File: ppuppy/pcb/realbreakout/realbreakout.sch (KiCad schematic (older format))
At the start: 18 parts, among them J1 Conn_01x36, J10 BCM11, J11 BCM13, J2 Conn_01x36, J3 Conn_01x36, J4 BCM25, J5 BCM24, J6 BCM27, J7 3V, J8 GND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

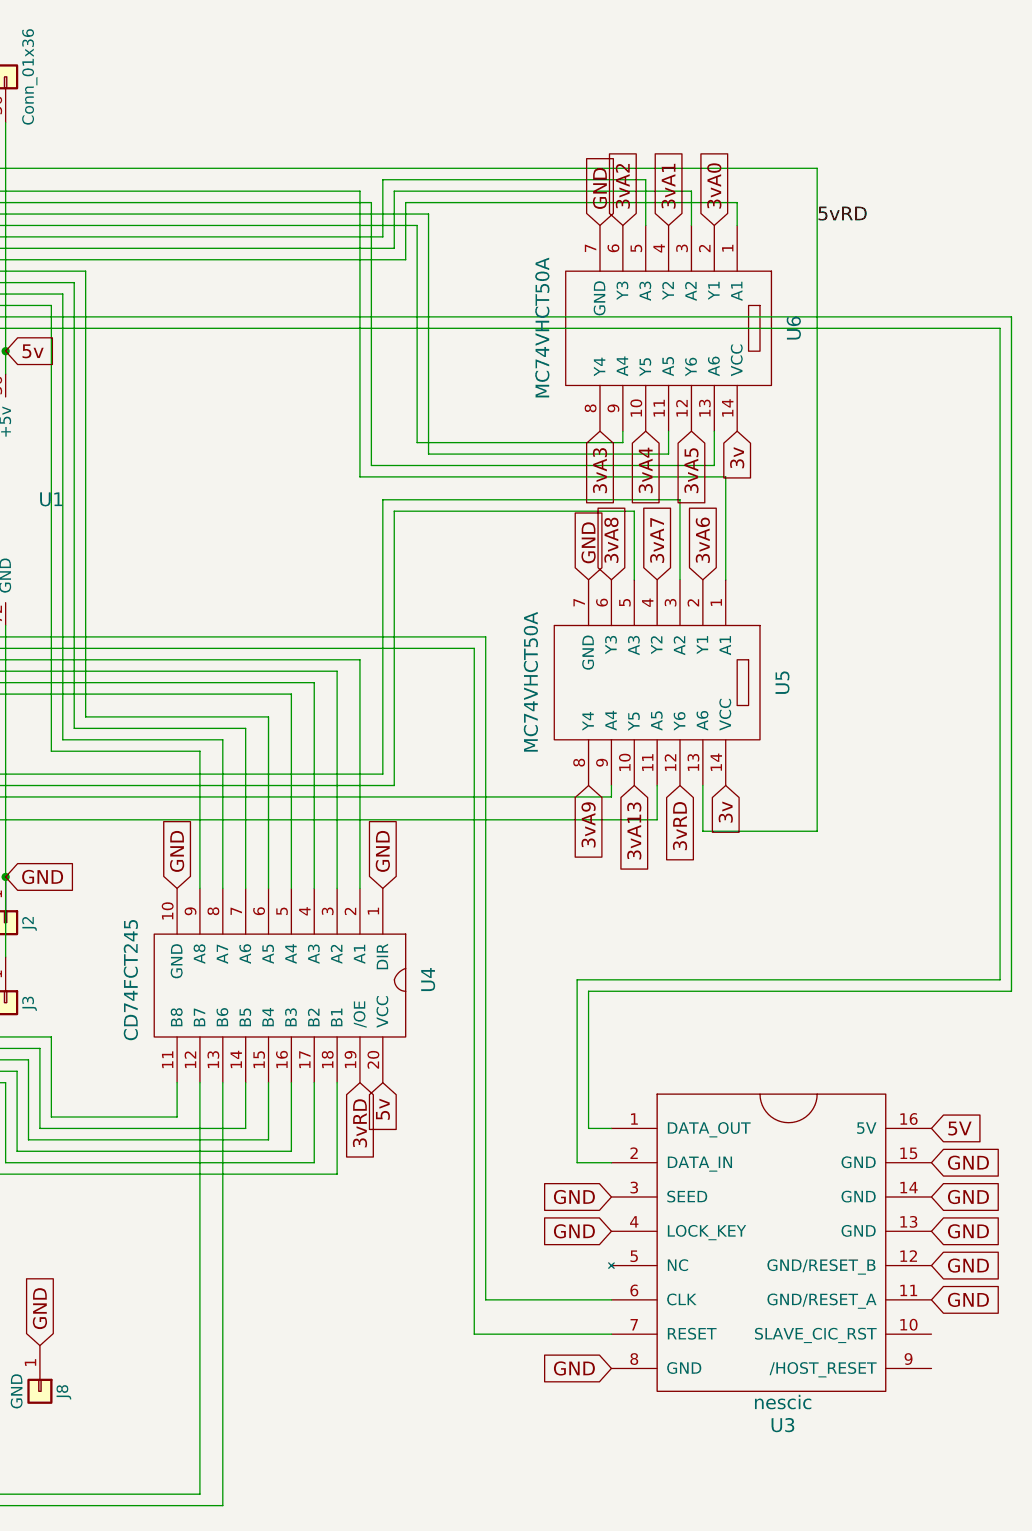
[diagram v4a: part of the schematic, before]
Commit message: Re-commit this stuff, which sourceforge lost (restoring a backup?\!?)
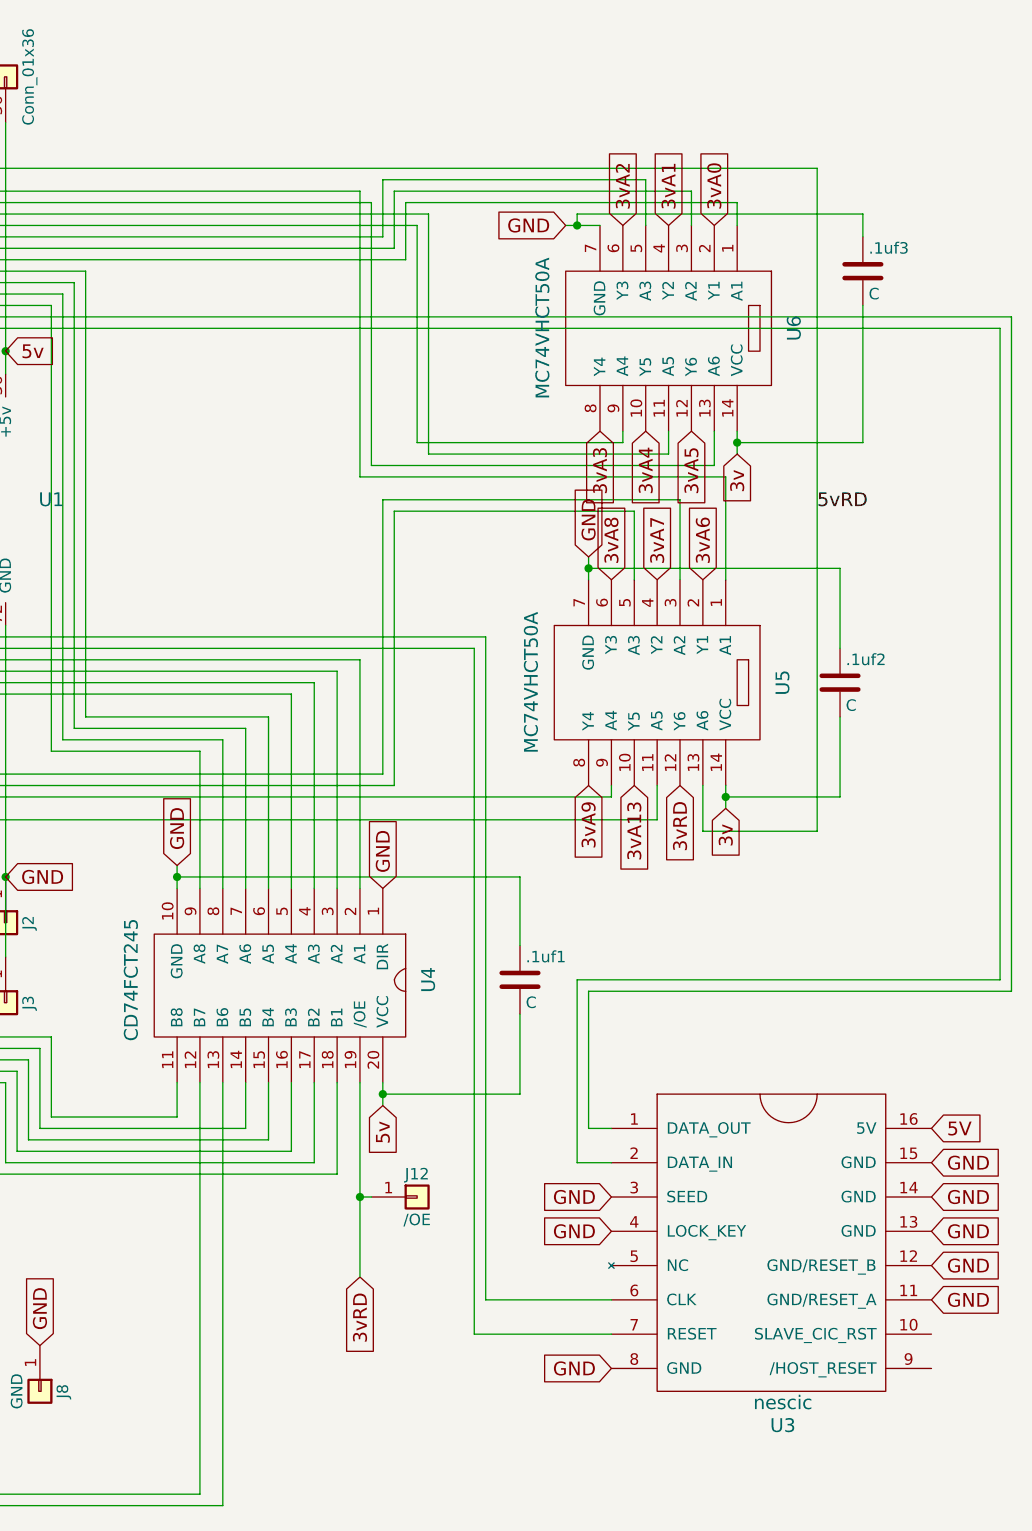
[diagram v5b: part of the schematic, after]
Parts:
- added .1uf1, .1uf2, .1uf3: C, Capacitors_THT:C_Disc_D5.0mm_W2.5mm_P5.00mm, symbol C
- added J12: /OE, Pin_Headers:Pin_Header_Straight_1x01_Pitch2.54mm, symbol Conn_01x01
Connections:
- net 3v: now also .1uf2.2, .1uf3.2
- net 3vRD: now also J12.1 (Pin_1)
- net 5v: now also .1uf1.2
- net GND: now also .1uf1.1, .1uf2.1, .1uf3.1
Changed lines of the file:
@@
 	0    1    1    0
 $EndComp
-Text GLabel 7450 3700 1    60   Input ~ 0
+Text GLabel 7450 3600 1    60   Input ~ 0
 GND
-Text GLabel 8350 4550 3    60   Input ~ 0
+Text GLabel 8350 4650 3    60   Input ~ 0
 5v
 Text GLabel 2150 1550 1    60   Input ~ 0
@@
 	0    1    1    0
 $EndComp
-Text GLabel 9900 1700 3    60   Input ~ 0
+Text GLabel 9900 1800 3    60   Input ~ 0
 3v
-Text GLabel 9850 3250 3    60   Input ~ 0
+Text GLabel 9850 3350 3    60   Input ~ 0
 3v
-Text GLabel 9250 2350 1    60   Input ~ 0
+Text GLabel 9250 2250 1    60   Input ~ 0
 GND
-Text GLabel 9300 800  1    60   Input ~ 0
+Text GLabel 9150 800  0    60   Input ~ 0
 GND
 Wire Wire Line
@@
 Text GLabel 5100 4700 1    60   Input ~ 0
 3v
-Text GLabel 8250 4550 3    60   Input ~ 0
+Text GLabel 8250 5400 3    60   Input ~ 0
 3vRD
 Wire Wire Line
@@
 Wire Wire Line
 	9750 3450 9750 3250
-Text Label 10250 800  0    60   ~ 0
+Text Label 10250 2050 0    60   ~ 0
 5vRD
 Text Label 1900 3300 0    60   ~ 0
@@
 Wire Wire Line
 	5000 4600 5000 4700
+$Comp
+L C .1uf2
+U 1 1 5AE8FA00
+P 10350 2800
+F 0 ".1uf2" H 10375 2900 50  0000 L CNN
+F 1 "C" H 10375 2700 50  0000 L CNN
+F 2 "Capacitors_THT:C_Disc_D5.0mm_W2.5mm_P5.00mm" H 10388 2650 50  0001 C CNN
+F 3 "" H 10350 2800 50  0001 C CNN
+	1    10350 2800
+	1    0    0    -1
+$EndComp
+Wire Wire Line
+	9850 3350 9850 3250
+Connection ~ 9850 3300
+Wire Wire Line
+	9850 3300 10350 3300
+Wire Wire Line
+	10350 3300 10350 2950
+Wire Wire Line
+	9250 2250 9250 2350
+Connection ~ 9250 2300
+Wire Wire Line
+	9250 2300 10350 2300
+Wire Wire Line
+	10350 2300 10350 2650
+Wire Wire Line
+	9150 800  9300 800
+Connection ~ 9200 800
+$Comp
+L C .1uf3
+U 1 1 5AE9096D
+P 10450 1000
+F 0 ".1uf3" H 10475 1100 50  0000 L CNN
+F 1 "C" H 10475 900 50  0000 L CNN
+F 2 "Capacitors_THT:C_Disc_D5.0mm_W2.5mm_P5.00mm" H 10488 850 50  0001 C CNN
+F 3 "" H 10450 1000 50  0001 C CNN
+	1    10450 1000
+	1    0    0    -1
+$EndComp
+Wire Wire Line
+	9900 1800 9900 1700
+Connection ~ 9900 1750
+Wire Wire Line
+	9900 1750 10450 1750
+Wire Wire Line
+	10450 1750 10450 1150
+Wire Wire Line
+	10450 850  10450 750
+Wire Wire Line
+	10450 750  9200 750
+Wire Wire Line
+	9200 750  9200 800
+Wire Wire Line
+	8350 4650 8350 4550
+Wire Wire Line
+	7450 3700 7450 3600
+Connection ~ 7450 3650
+Connection ~ 8350 4600
+$Comp
+L C .1uf1
+U 1 1 5AE9161B
+P 8950 4100
+F 0 ".1uf1" H 8975 4200 50  0000 L CNN
+F 1 "C" H 8975 4000 50  0000 L CNN
+F 2 "Capacitors_THT:C_Disc_D5.0mm_W2.5mm_P5.00mm" H 8988 3950 50  0001 C CNN
+F 3 "" H 8950 4100 50  0001 C CNN
+	1    8950 4100
+	1    0    0    -1
+$EndComp
+Wire Wire Line
+	7450 3650 8950 3650
+Wire Wire Line
+	8950 3650 8950 3950
+Wire Wire Line
+	8350 4600 8950 4600
+Wire Wire Line
+	8950 4600 8950 4250
+$Comp
+L Conn_01x01 J12
+U 1 1 5AE92E68
+P 8500 5050
+F 0 "J12" H 8500 5150 50  0000 C CNN
+F 1 "/OE" H 8500 4950 50  0000 C CNN
+F 2 "Pin_Headers:Pin_Header_Straight_1x01_Pitch2.54mm" H 8500 5050 50  0001 C CNN
+F 3 "" H 8500 5050 50  0001 C CNN
+	1    8500 5050
+	1    0    0    -1
+$EndComp
+Wire Wire Line
+	8250 4550 8250 5400
+Wire Wire Line
+	8300 5050 8250 5050
+Connection ~ 8250 5050
 $EndSCHEMATC

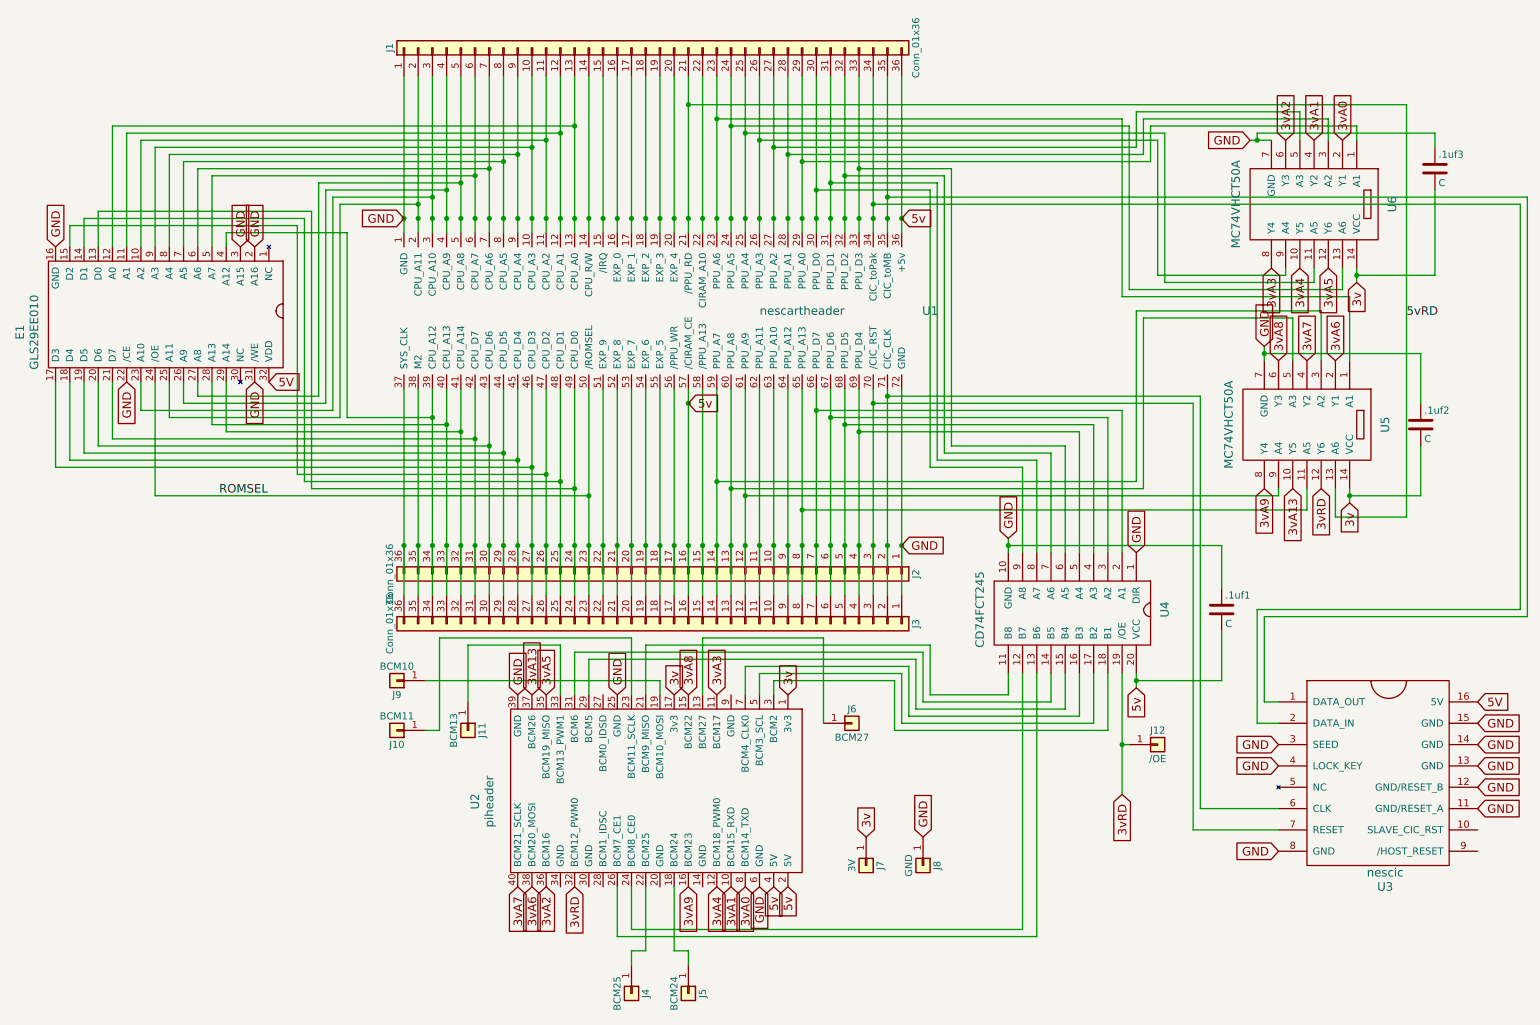
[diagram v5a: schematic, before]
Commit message: Cart plays sound for debugging when video is not present. Fix circuit board layout
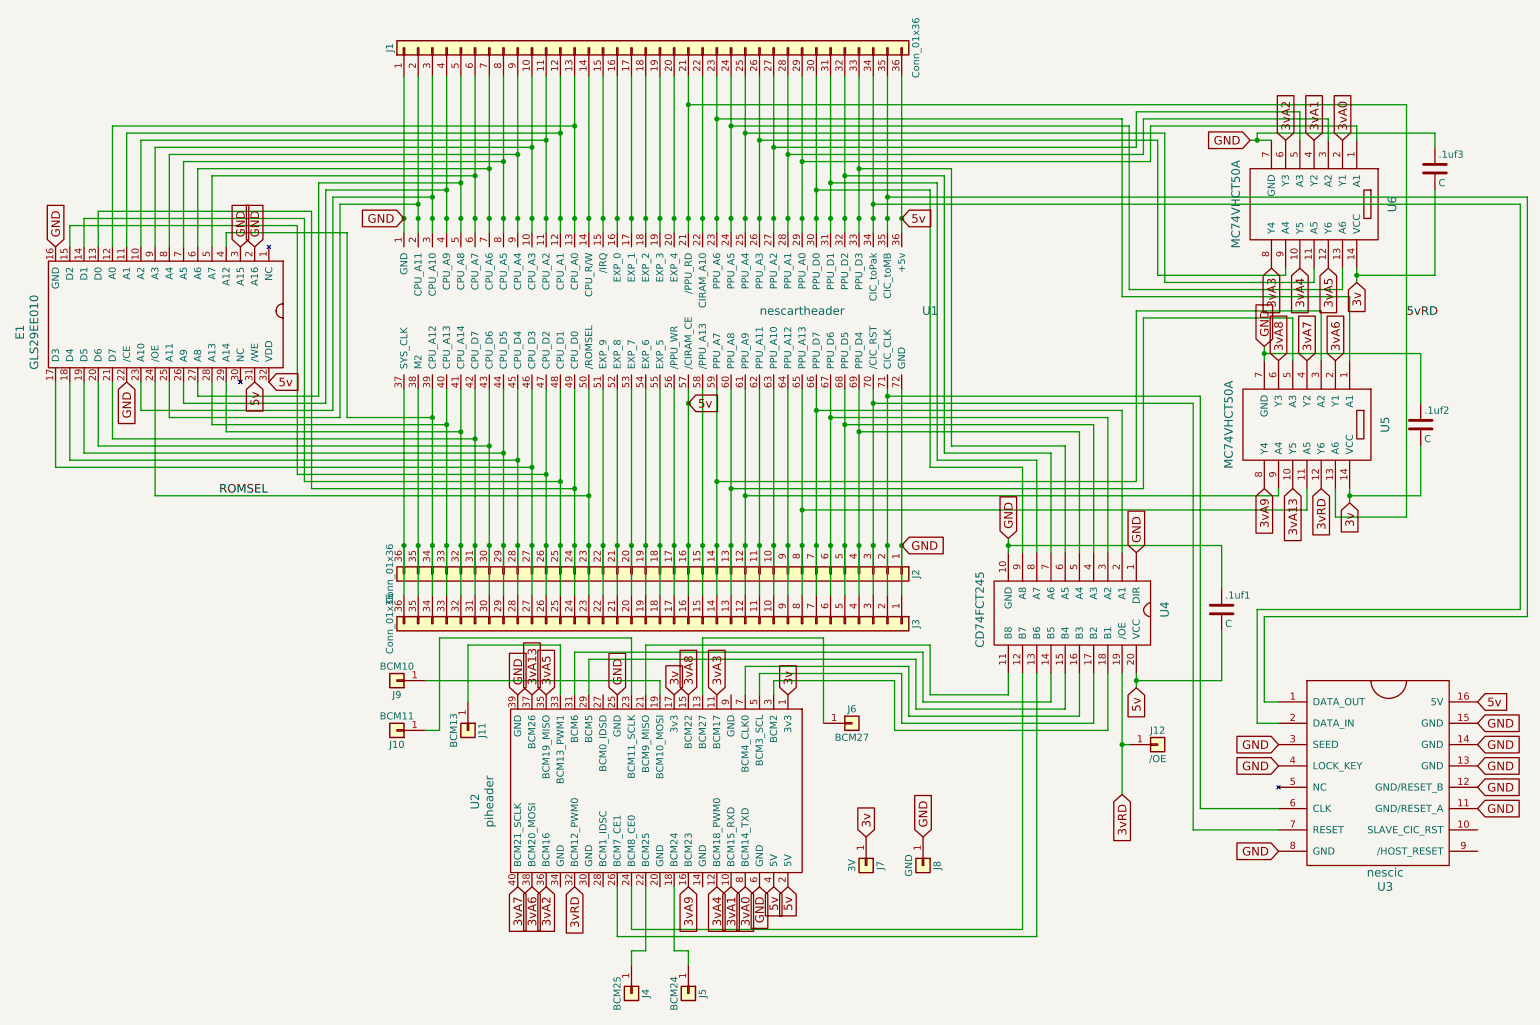
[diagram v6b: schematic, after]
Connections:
- net 5V is gone; now on net 5v: E1.32 (VDD), U3.16 (5V)
- net 5v: now also E1.31 (/WE)
- net GND: no longer E1.31 (/WE)
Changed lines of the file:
@@
 GND
 Text GLabel 2250 2500 2    60   Input ~ 0
-5V
+5v
 $Comp
 L nescic U3
@@
 GND
 Text GLabel 10750 4750 2    60   Input ~ 0
-5V
+5v
 Text GLabel 10750 5200 2    60   Input ~ 0
 GND
@@
 GND
 Text GLabel 2050 1550 1    60   Input ~ 0
-GND
-Text GLabel 2150 2500 3    60   Input ~ 0
 GND
 Text GLabel 1250 2500 3    60   Input ~ 0
@@
 	8300 5050 8250 5050
 Connection ~ 8250 5050
+Text GLabel 2150 2500 3    60   Input ~ 0
+5v
 $EndSCHEMATC
